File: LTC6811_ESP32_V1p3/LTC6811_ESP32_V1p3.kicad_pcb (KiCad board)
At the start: 2 copper layers, 150 x 90 mm, 262 parts, among them J1 PB MB, J10 Hole /NC, J11 Hole /NC, J12 Hole /NC, J13 B7B-XH-A, J14 B7B-XH-A, J15 PB MB, J2 OLED /NC, J3 CAN /NC, J4 USB, J5 UART /NC, J6 JTAG /NC, J8 SERIAL /NC, J9 Hole /NC, Q1 BSS138, Q10 TSM2323, Q11 TSM2323, Q12 TSM2323, Q13 TSM2323, Q14 TSM2323, Q2 NSV1C201MZ4, Q3 TSM2323, Q4 TSM2323, Q5 TSM2323, Q6 TSM2323, Q7 TSM2323, Q8 TSM2323, Q9 TSM2323, U1 TPS76350, U10 CP2104, U11 ISO1050DUBR, U12 LTC6811HG-1, U2 AMC1301 or AMC1302, U3 AMC1301, U4 SN6501DBV, U5 OPA2197IDR, U6 ISL28022, U7 LMR51420XDDCR, U8 ESP32-DevKitC V4, U9 LTC6820

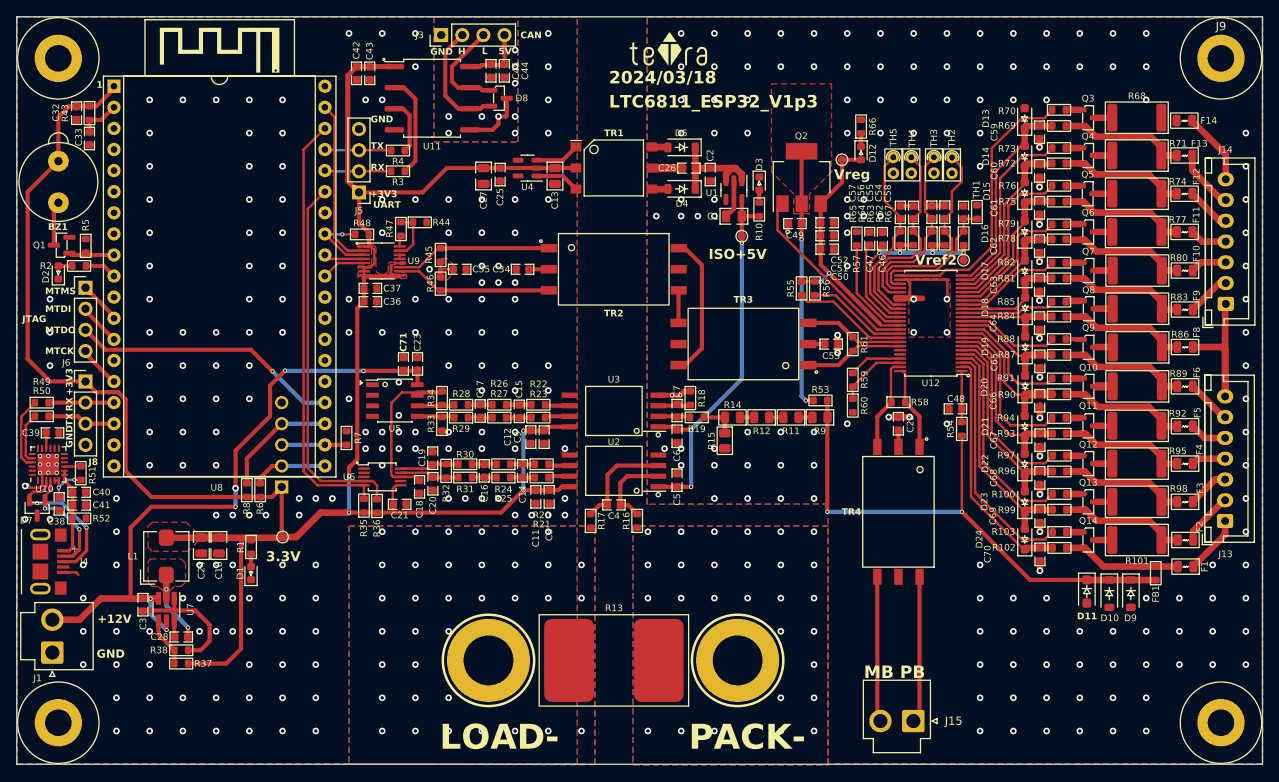
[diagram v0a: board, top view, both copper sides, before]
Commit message: Optimize signal transmission lines.
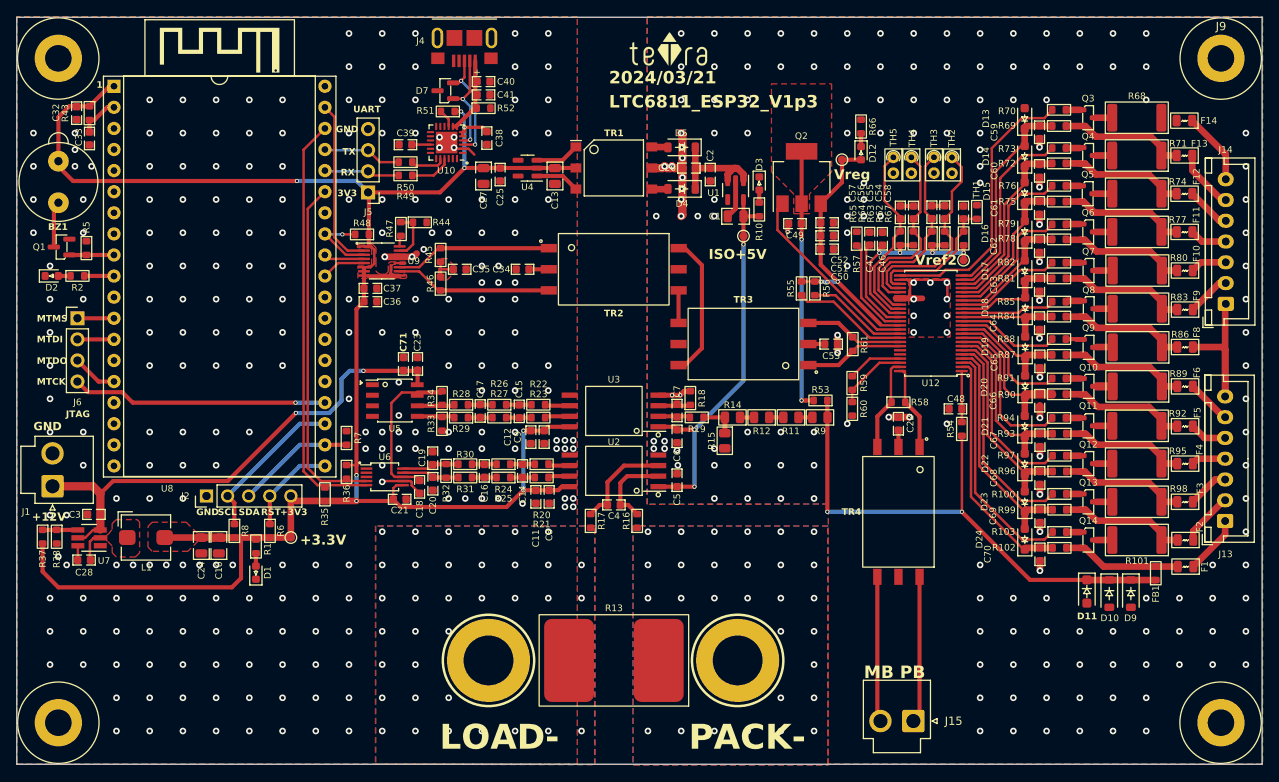
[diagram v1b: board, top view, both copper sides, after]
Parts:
- removed C42, C44: 1uF/25V, Capacitor_SMD:C_0603_1608Metric
- removed C43, C45: 100nF/100V, Capacitor_SMD:C_0603_1608Metric
- removed D8: ESD24VS2U, Package_TO_SOT_SMD:SOT-23
- removed J3: CAN /NC, Connector_PinHeader_2.54mm:PinHeader_1x04_P2.54mm_Vertical
- removed J8: SERIAL /NC, Connector_PinHeader_2.54mm:PinHeader_1x04_P2.54mm_Vertical
- removed R3, R4: 0, Resistor_SMD:R_0603_1608Metric
- removed U11: ISO1050DUBR, Package_SO:SOP-8_6.62x9.15mm_P2.54mm
- J2: moved to F.Cu
- R49, R50: value 240R -> 0
- moved J4 80.6 mm to (117.0, 53.4), turned to 180 degrees
- moved D7 70.3 mm to (114.7, 59.4), turned to 180 degrees
- moved C40 69.4 mm to (119.3, 58.3)
- moved R52 69.4 mm to (119.3, 61.5)
- moved C41 69.4 mm to (119.3, 59.9)
- moved C38 67.8 mm to (119.7, 65.1)
- moved R51 62.1 mm to (115.0, 61.9), turned to 180 degrees
- moved U10 61.7 mm to (114.8, 65.6), turned to 180 degrees
- moved C39 54.9 mm to (109.9, 65.9), turned to 180 degrees
- moved R50 53.4 mm to (109.9, 68.0), turned to 180 degrees
- moved R49 51.6 mm to (109.9, 69.6), turned to 180 degrees
- moved R37 22.6 mm to (66.2, 113.1), turned to -90 degrees
- moved R38 20.3 mm to (67.9, 113.1), turned to -90 degrees
- moved J1 20.0 mm to (67.4, 107.0)
- moved C28 14.9 mm to (71.2, 115.9)
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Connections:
- C38 pad 1: VDD -> +3V3
- J1 pad 1: GND -> +12V
- J1 pad 2: +12V -> GND
- J2 pad 1: +3V3 -> GND
- J2 pad 2: /MCU/OLED_RST -> /MCU/OLED_SCL
- J2 pad 4: /MCU/OLED_SCL -> /MCU/OLED_RST
- J2 pad 5: GND -> +3V3
- J5 pad 2: /MCU/CAN_RX -> /MCU/RX_USB
- J5 pad 3: /MCU/CAN_TX -> /MCU/TX_USB
- J6 pad 3: /MCU/MTDO -> /MCU/MTCK
- J6 pad 4: /MCU/MTCK -> /MCU/MTDO
- R51 pad 1: VDD -> +3V3
- U10 pad 5: VDD -> +3V3
- U10 pad 6: VDD -> +3V3
- U8 pad 16: /MCU/RX_USB -> unconnected-(U8-SD2-Pad16)
- U8 pad 17: /MCU/TX_USB -> unconnected-(U8-SD3-Pad17)
- U8 pad 34: /MCU/CAN_RX -> /MCU/RX_USB
- U8 pad 35: /MCU/CAN_TX -> /MCU/TX_USB
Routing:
- net +3V3: track 274.0 -> 243.0 mm, vias 4 -> 8
- net +12V: track 78.4 -> 61.1 mm, vias 6 -> 2
- net /CAN/CANH: track 14.5 -> 0.00 mm
- net /CAN/CAN_RX: track 12.3 -> 0.00 mm
- net /CAN/CANL: track 12.3 -> 0.00 mm
- net GND_PACK: track 51.4 -> 62.5 mm, vias 185 -> 202
- net GND: track 23.5 -> 14.3 mm, vias 183 -> 231
- net /MCU/CAN_TX: track 8.11 -> 0.00 mm
- net /MCU/CAN_RX: track 8.09 -> 0.00 mm
- net /CAN/5V_CAN: track 7.83 -> 0.00 mm
- net /CAN/CAN_GND: track 7.81 -> 0.00 mm, vias 9 -> 0
- net /CAN/CAN_TX: track 6.64 -> 0.00 mm
- net /MCU/OLED_SDA: track 7.80 -> 14.3 mm
- net VDD: track 5.61 -> 0.00 mm, vias 2 -> 0
- net Net-(U7-SW): track 9.26 -> 3.68 mm, vias 2 -> 0
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- removed copper zone on B.Cu, net /CAN/CAN_GND
- removed copper zone on F.Cu, net /CAN/CAN_GND
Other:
- board text added: "+3.3V"
- board text added: "2024/03/21"
- board text added: "3V3"
- board text removed: "2024/03/18"
- board text removed: "3.3V"
- board text removed: "5V"
- board text removed: "CAN"
- board text removed: "H"
- board text removed: "L"

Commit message: Add files via upload
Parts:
- BAT-1, BAT1: footprint Battery:Battery_6mm×10mm_Cell_half_2 -> Library:Battery_6mm×10mm_Cell_half_2
- BZ1: footprint Buzzer_Beeper:Beeper_AI-1027-TWT-5V -> Library:Beeper_AI-1027-TWT-5V
- C1, C10, C13, C24, C27: footprint Capacitor_SMD:C_0805_2012Metric -> Library:C_0805_2012Metric
- C11, C12, C14, C15, C16, C17, C18, C19, C2, C20, C21, C22, C23, C25, C26, C28, C3, C32, C33, C34, C35, C36, C37, C38, C39, C4, C40, C41, C46, C47, C48, C49, C5, C50, C51, C52, C53, C54, C55, C56, C57, C58, C59, C6, C60, C61, C62, C63, C64, C65, C66, C67, C68, C69, C7, C70, C71, C8, C9: footprint Capacitor_SMD:C_0603_1608Metric -> Library:C_0603_1608Metric
- D1, D12, D2, D3: footprint LED_SMD:LED_0603_1608Metric -> Library:LED_0603_1608Metric
- D10, D4, D5, D9: footprint Diode_SMD:D_SOD-123 -> Library:D_SOD-123
- D11: footprint Diode_SMD:D_SOD-123F -> Library:D_SOD-123F
- D13, D14, D15, D16, D17, D18, D19, D20, D21, D22, D23, D24: footprint Diode_SMD:D_SOD-323_HandSoldering -> Library:D_SOD-323_HandSoldering
- D7, Q1, Q10, Q11, Q12, Q13, Q14, Q3, Q4, Q5, Q6, Q7, Q8, Q9: footprint Package_TO_SOT_SMD:SOT-23 -> Library:SOT-23
- F1, F10, F11, F12, F13, F14, F2, F3, F4, F5, F6, F8, F9: footprint Fuse:Fuse_0805_2012Metric -> Library:Fuse_0805_2012Metric
- FB1, R1, R10, R100, R102, R103, R16, R17, R18, R19, R2, R20, R21, R22, R23, R24, R25, R26, R27, R28, R29, R30, R31, R32, R33, R34, R35, R36, R37, R38, R43, R44, R45, R46, R47, R48, R49, R5, R50, R51, R52, R53, R54, R55, R56, R57, R59, R6, R60, R61, R62, R63, R64, R65, R66, R67, R69, R7, R70, R72, R73, R75, R76, R78, R79, R8, R81, R82, R84, R85, R87, R88, R90, R91, R93, R94, R96, R97, R99, TH1: footprint Resistor_SMD:R_0603_1608Metric -> Library:R_0603_1608Metric
- J1, J15: footprint Connector_JST:JST_VH_B2P-VH-B_1x02_P3.96mm_Vertical -> Library:JST_VH_B2P-VH-B_1x02_P3.96mm_Vertical
- J10, J11, J12, J9: footprint MountingHole:MountingHole_3.2mm_M3_ISO7380_Pad -> Library:MountingHole_3.2mm_M3_ISO7380_Pad
- J13, J14: footprint Connector_JST:JST_XH_B7B-XH-A_1x07_P2.50mm_Vertical_BAT_6S -> Library:JST_XH_B7B-XH-A_1x07_P2.50mm_Vertical_BAT_6S
- J2: footprint Connector_PinHeader_2.54mm:PinHeader_1x05_P2.54mm_Vertical -> Library:PinHeader_1x05_P2.54mm_Vertical
- J4: footprint Connector_USB:Micro_USB_B-2013499-1 -> Library:Micro_USB_B-2013499-1
- J5, J6: footprint Connector_PinHeader_2.54mm:PinHeader_1x04_P2.54mm_Vertical -> Library:PinHeader_1x04_P2.54mm_Vertical
- L1: footprint Inductor_SMD:L_Bourns_SRP5030T -> Library:L_Bourns_SRP5030T
- LOGO1: footprint Symbol:teTra-LOGO -> Library:teTra-LOGO
- Q2: footprint Package_TO_SOT_SMD:SOT-223 -> Library:SOT-223
- R101, R68, R71, R74, R77, R80, R83, R86, R89, R92, R95, R98: footprint Resistor_SMD:R_2512_6332Metric -> Library:R_2512_6332Metric
- R11, R12, R14, R15, R9: footprint Resistor_SMD:R_0805_2012Metric -> Library:R_0805_2012Metric
- R13: footprint Resistor_SMD:R_PSR500HTQFB0L10_Metric_Pad5.2x8.75mm_HandSolder -> Library:R_PSR500HTQFB0L10_Metric_Pad5.2x8.75mm_HandSolder
- R58: value 100K -> 100R; footprint Resistor_SMD:R_0603_1608Metric -> Library:R_0603_1608Metric
- TH2, TH3, TH4, TH5: footprint Resistor_THT:R_Axial_DIN0204_L3.6mm_D1.6mm_P1.90mm_Vertical -> Library:R_Axial_DIN0204_L3.6mm_D1.6mm_P1.90mm_Vertical
- TP1, TP2, TP3, TP4: footprint TestPoint:TestPoint_Pad_D1.0mm -> Library:TestPoint_Pad_D1.0mm
- TR1: footprint Connector_Wuerth:WURTH-760390015 -> Library:WURTH-760390015
- TR2, TR3, TR4: footprint Transformer_SMD:HM2108NL -> Library:HM2108NL
- U1, U4: footprint Package_TO_SOT_SMD:SOT-23-5 -> Library:SOT-23-5
- U10: footprint Package_DFN_QFN:HVQFN-24-1EP_4x4mm_P0.5mm_EP2.6x2.6mm -> Library:HVQFN-24-1EP_4x4mm_P0.5mm_EP2.6x2.6mm
- U12: footprint Package_SO:TSSOP-48_6.1x12.5mm_P0.5mm -> Library:TSSOP-48_6.1x12.5mm_P0.5mm
- U2, U3: footprint Package_SO:SSO-8_6.8x5.9mm_P1.27mm_Clearance8mm -> Library:SSO-8_6.8x5.9mm_P1.27mm_Clearance8mm
- U5: footprint PCM_4ms_Package_SOIC:SOIC-8_3.9x4.9mm_Pitch1.27mm -> Library:SOIC-8_3.9x4.9mm_Pitch1.27mm
- U6: footprint PCM_4ms_Package_SSOP:MSOP-10_3x3mm_P0.5mm -> Library:MSOP-10_3x3mm_P0.5mm
- U7: footprint Package_TO_SOT_SMD:SOT-23-6_Handsoldering -> Library:SOT-23-6_Handsoldering
- U8: footprint RF_Module:ESP32-DevKitc V4_DIP-38_27.9mm×48.2mm -> Library:ESP32-DevKitc V4_DIP-38_27.9mm×48.2mm
- U9: footprint Package_SO:MSOP-16_3x4mm_P0.5mm -> Library:MSOP-16_3x4mm_P0.5mm
- turned R58 to 180 degrees
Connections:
- R58 pad 1: /LTC6811/IMB -> /LTC6811/IPB
- R58 pad 2: /LTC6811/IPB -> /LTC6811/IMB
